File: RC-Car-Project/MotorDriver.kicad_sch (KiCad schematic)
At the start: 14 parts, among them Q1 BTN8982TA, Q2 BTN8982TA, Q5 BTN8982TA, Q6 BTN8982TA, U9 SN74HC244PWR

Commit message: Fixed Drivers
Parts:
- added R32, R33, R34, R35: 10k, Resistor_SMD:R_0201_0603Metric, symbol Device:R
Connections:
- net MOTOR_2_L_EN is gone; now on net MOTOR_1_L_PWM: U9.2 (1A1)
- net MOTOR_2_R_EN is gone; now on net MOTOR_2_L_PWM: U9.6 (1A3)
- net +3V3: now also Q1.3 (INH), Q2.3 (INH), Q5.3 (INH), Q6.3 (INH)
- net GND_3V3: now also R32.1, R33.1, R34.1, R35.1; no longer U9.1 (*1OE)
- net MOTOR_1_L_PWM: no longer U9.13 (2A2)
- net MOTOR_1_R_PWM: now also U9.4 (1A2); no longer U9.17 (2A4)
- net MOTOR_2_L_PWM: no longer U9.4 (1A2)
- net at U9.12 (1Y4): now also Q6.2 (IN), R35.2; no longer Q2.2 (IN)
- net at U9.14 (1Y3): now also Q5.2 (IN), R34.2; no longer Q2.3 (INH)
- net at U9.7 (2Y2): no longer Q5.2 (IN)
- net at U9.9 (2Y1): no longer Q5.3 (INH)
- net at U9.16 (1Y2): now also Q2.2 (IN), R33.2; no longer Q1.2 (IN)
- net at U9.18 (1Y1): now also Q1.2 (IN), R32.2; no longer Q1.3 (INH)
- net at U9.3 (2Y4): no longer Q6.2 (IN)
- net at U9.5 (2Y3): no longer Q6.3 (INH)
- net MOTOR_1_L_EN: no longer names the net of U9.11 (2A1)
- net MOTOR_1_R_EN: no longer names the net of U9.15 (2A3)
- new net MOTOR_EN: U9.1 (*1OE)
- no-connect marks 4 -> 12
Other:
- moved on the sheet: C13, U9

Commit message: Fixed Annotations
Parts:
- C44: renamed from C13; footprint Capacitor_SMD:C_0201_0603Metric -> Capacitor_SMD:C_0603_1608Metric
- C45: renamed from C6; footprint Capacitor_SMD:C_0201_0603Metric -> Capacitor_SMD:C_0603_1608Metric
- C46: renamed from C5; footprint Capacitor_SMD:C_0201_0603Metric -> Capacitor_SMD:C_0603_1608Metric
- C47: renamed from C41; footprint Capacitor_SMD:C_0201_0603Metric -> Capacitor_SMD:C_0603_1608Metric
- C48: renamed from C42; footprint Capacitor_SMD:C_0201_0603Metric -> Capacitor_SMD:C_0603_1608Metric
- R22: renamed from R35; footprint Resistor_SMD:R_0201_0603Metric -> Resistor_SMD:R_0603_1608Metric
- R23: renamed from R32; footprint Resistor_SMD:R_0201_0603Metric -> Resistor_SMD:R_0603_1608Metric
- R24: renamed from R33; footprint Resistor_SMD:R_0201_0603Metric -> Resistor_SMD:R_0603_1608Metric
- R25: renamed from R34; footprint Resistor_SMD:R_0201_0603Metric -> Resistor_SMD:R_0603_1608Metric
- R26: renamed from R6; footprint Resistor_SMD:R_0201_0603Metric -> Resistor_SMD:R_0603_1608Metric
- R27: renamed from R5; footprint Resistor_SMD:R_0201_0603Metric -> Resistor_SMD:R_0603_1608Metric
- R28: renamed from R17; footprint Resistor_SMD:R_0201_0603Metric -> Resistor_SMD:R_0603_1608Metric
- R29: renamed from R18; footprint Resistor_SMD:R_0201_0603Metric -> Resistor_SMD:R_0603_1608Metric
- renumbered Q5 to Q3, Q6 to Q4

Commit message: Changed
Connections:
- net MOTOR_1_L_PWM: now also U9.4 (1A2); no longer U9.2 (1A1)
- net MOTOR_1_R_PWM: now also U9.2 (1A1); no longer U9.4 (1A2)
- net at Q2.2 (IN), R24.2: now also U9.18 (1Y1); no longer U9.16 (1Y2)
- net at Q1.2 (IN), R23.2: now also U9.16 (1Y2); no longer U9.18 (1Y1)
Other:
- moved on the sheet: C45, C46, Q1, Q2, R23, R24, R26, R27

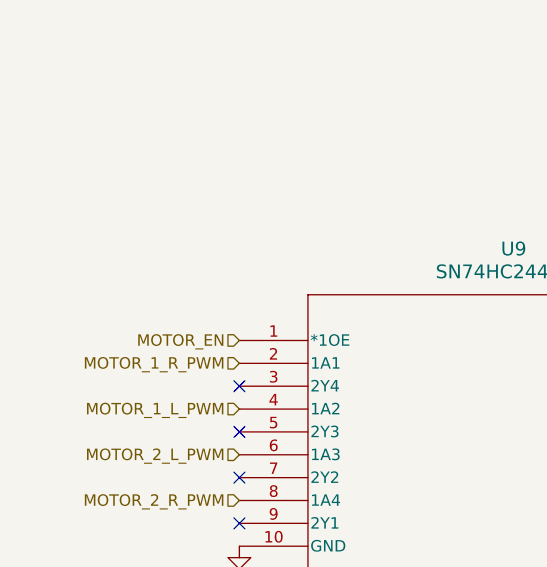
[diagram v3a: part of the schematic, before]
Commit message: Redid Screwholes
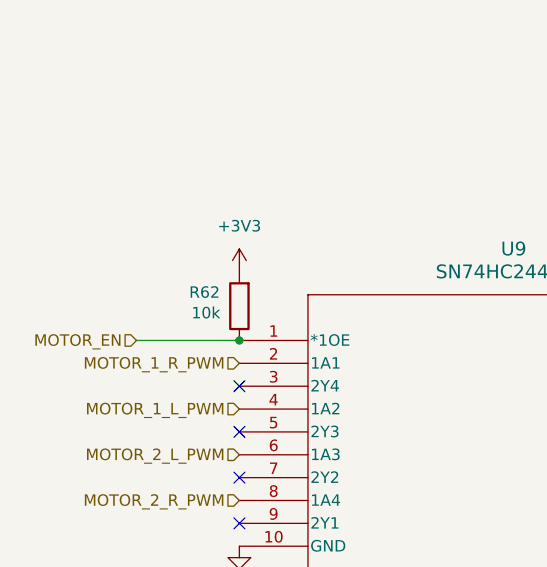
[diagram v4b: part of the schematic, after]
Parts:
- added R62: 10k, Resistor_SMD:R_0603_1608Metric, symbol Device:R
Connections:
- net +3V3: now also R62.2
- net MOTOR_EN: now also R62.1
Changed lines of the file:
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@@
+	)
+	(junction
+		(at 69.85 71.12)
+		(diameter 0)
+		(color 0 0 0 0)
 	)
 	(junction
@@
 	(wire
 		(pts
+			(xy 58.42 71.12) (xy 69.85 71.12)
+		)
+		(stroke
+			(width 0)
+			(type default)
+		)
+	)
+	(wire
+		(pts
 			(xy 190.5 148.59) (xy 196.85 148.59)
 		)
@@
 	(hierarchical_label "MOTOR_EN"
 		(shape input)
-		(at 69.85 71.12 180)
+		(at 58.42 71.12 180)
 		(fields_autoplaced yes)
 		(effects
@@
 	)
 	(symbol
+		(lib_id "Device:R")
+		(at 69.85 67.31 180)
+		(unit 1)
+		(exclude_from_sim no)
+		(in_bom yes)
+		(on_board yes)
+		(dnp no)
+		(property "Reference" "R62"
+			(at 64.262 65.786 0)
+			(effects
+				(font
+					(size 1.27 1.27)
+				)
+				(justify right)
+			)
+		)
+		(property "Value" "10k"
+			(at 64.516 68.072 0)
+			(effects
+				(font
+					(size 1.27 1.27)
+				)
+				(justify right)
+			)
+		)
+		(property "Footprint" "Resistor_SMD:R_0603_1608Metric"
+			(at 71.628 67.31 90)
+			(effects
+				(font
+					(size 1.27 1.27)
+				)
+				(hide yes)
+			)
+		)
+		(property "Datasheet" "~"
+			(at 69.85 67.31 0)
+			(effects
+				(font
+					(size 1.27 1.27)
+				)
+				(hide yes)
+			)
+		)
+		(property "Description" "Resistor"
+			(at 69.85 67.31 0)
+			(effects
+				(font
+					(size 1.27 1.27)
+				)
+				(hide yes)
+			)
+		)
+		(pin "2"
+		)
+		(pin "1"
+		)
+		(instances
+			(project "RC-Car-Project"
+				(path "/ba870fd1-751d-4755-8e1a-1ea86ca9e2f6/15913cf9-3929-404b-bf1a-e176e0fdf251"
+					(reference "R62")
+					(unit 1)
+				)
+			)
+		)
+	)
+	(symbol
 		(lib_id "power:GNDA")
 		(at 215.9 41.91 0)
@@
 					(unit 1)
 				)
+			)
+		)
+	)
+	(symbol
+		(lib_id "power:+3V3")
+		(at 69.85 63.5 0)
+		(unit 1)
+		(exclude_from_sim no)
+		(in_bom yes)
+		(on_board yes)
+		(dnp no)
+		(fields_autoplaced yes)
+		(property "Reference" "#PWR0142"
+			(at 69.85 67.31 0)
+			(effects
+				(font
+					(size 1.27 1.27)
+				)
+				(hide yes)
+			)
+		)
+		(property "Value" "+3V3"
+			(at 69.85 58.42 0)
+			(effects
+				(font
+					(size 1.27 1.27)
+				)
+			)
+		)
+		(property "Footprint" ""
+			(at 69.85 63.5 0)
+			(effects
+				(font
+					(size 1.27 1.27)
+				)
+				(hide yes)
+			)
+		)
+		(property "Datasheet" ""
+			(at 69.85 63.5 0)
+			(effects
+				(font
+					(size 1.27 1.27)
+				)
+				(hide yes)
+			)
+		)
+		(property "Description" "Power symbol creates a global label with name \"+3V3\""
+			(at 69.85 63.5 0)
+			(effects
+				(font
+					(size 1.27 1.27)
+				)
+				(hide yes)
+			)
+		)
+		(pin "1"
+		)
+		(instances
+			(project "RC-Car-Project"
+				(path "/ba870fd1-751d-4755-8e1a-1ea86ca9e2f6/15913cf9-3929-404b-bf1a-e176e0fdf251"
+					(reference "#PWR0142")
+					(unit 1)
+				)

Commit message: Fixed Resistors
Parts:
- added R64, R65, R66, R67, R72: 10k, Resistor_SMD:R_0603_1608Metric, symbol Device:R
- added R68, R69, R70, R71: 1k, Resistor_SMD:R_0603_1608Metric, symbol Device:R
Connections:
- net +3V3: now also R64.2, R65.2, R66.2, R67.2, R72.1; no longer Q1.3 (INH), Q2.3 (INH), Q3.3 (INH), Q4.3 (INH), U9.19 (*2OE)
- net GND_3V3: now also R68.2, R69.2, R70.2, R71.2
- net at Q2.6 (IS): now also R69.1
- net at Q3.6 (IS): now also R70.1
- net at Q1.6 (IS): now also R68.1
- net at Q4.6 (IS): now also R71.1
- new net: Q2.3 (INH), R64.1
- new net: Q4.3 (INH), R67.1
- new net: Q3.3 (INH), R66.1
- new net: Q1.3 (INH), R65.1
- new net: R72.2, U9.19 (*2OE)
- no-connect marks 12 -> 8

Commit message: Add caps
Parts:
- C44: MANUF_PN (none) -> C0603C104K5RAC7411
- C45, C46, C47, C48: value 0.1uF/25V -> 0.1uF/10V; MANUF_PN (none) -> C0603C104K5RAC7411
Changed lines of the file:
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@@
 			)
 		)
-		(property "MANUF_PN" ""
+		(property "MANUF_PN" "C0603C104K5RAC7411"
 			(at 144.78 64.77 0)
 			(effects
@@
 			)
 		)
-		(property "Value" "0.1uF/25V"
+		(property "Value" "0.1uF/10V"
 			(at 191.262 78.486 0)
 			(effects
@@
 			)
 		)
-		(property "MANUF_PN" ""
+		(property "MANUF_PN" "C0603C104K5RAC7411"
 			(at 190.5 76.2 0)
 			(effects
@@
 			)
 		)
-		(property "Value" "0.1uF/25V"
+		(property "Value" "0.1uF/10V"
 			(at 194.31 114.2999 0)
 			(effects
@@
 			)
 		)
-		(property "MANUF_PN" ""
+		(property "MANUF_PN" "C0603C104K5RAC7411"
 			(at 190.5 113.03 0)
 			(effects
@@
 			)
 		)
-		(property "Value" "0.1uF/25V"
+		(property "Value" "0.1uF/10V"
 			(at 194.31 39.3699 0)
 			(effects
@@
 			)
 		)
-		(property "MANUF_PN" ""
+		(property "MANUF_PN" "C0603C104K5RAC7411"
 			(at 190.5 38.1 0)
 			(effects
@@
 			)
 		)
-		(property "Value" "0.1uF/25V"
+		(property "Value" "0.1uF/10V"
 			(at 194.31 146.0499 0)
 			(effects
@@
 			)
 		)
-		(property "MANUF_PN" ""
+		(property "MANUF_PN" "C0603C104K5RAC7411"
 			(at 190.5 144.78 0)
 			(effects
